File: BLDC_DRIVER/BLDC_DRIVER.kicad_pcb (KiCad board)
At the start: 2 copper layers, 187 parts, among them IC101 DRV8323SRTAR, J1 XT60, J104 691311400103, J2 Conn_01x03_Pin, J3 Conn_01x03_Pin, J4 Conn_01x06_Pin, Q101 BSC146N10LS5ATMA1, Q102 BSC146N10LS5ATMA1, Q103 BSC146N10LS5ATMA1, Q104 BSC146N10LS5ATMA1, Q105 BSC146N10LS5ATMA1, Q106 BSC146N10LS5ATMA1, SW1 SW_Push_Dual_x2, SW2 SW_Push_Dual_x2, SW3 SW_Push_Dual_x2, SW4 SW_Push_Dual_x2, SW5 SW_Push_Dual_x2, U1 LDI1117-3.3H, U2 ESP32-S3-WROOM-1U-N16R2, U3 LMR51610YDBVR, U4 STM32G431RBTx, Y1 24MHz

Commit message: pcb update
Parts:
- moved Q101 119.0 mm to (159.8, 27.8), turned to 180 degrees
- moved Q103 118.2 mm to (173.5, 27.9), turned to 180 degrees
- moved Q105 118.2 mm to (187.9, 27.9), turned to 180 degrees
- moved R121 113.1 mm to (154.1, 36.0), turned to -90 degrees
- moved R122 109.7 mm to (150.1, 36.0), turned to -90 degrees
- moved Q102 105.1 mm to (153.1, 27.2)
- moved Q104 104.8 mm to (167.3, 27.3)
- moved Q106 104.7 mm to (181.7, 27.3)
- moved C105 103.6 mm to (129.9, 76.4), turned to 180 degrees
- moved C103 101.7 mm to (130.1, 31.6), turned to 180 degrees
- moved C106 101.7 mm to (130.0, 61.9), turned to 180 degrees
- moved C104 101.6 mm to (129.9, 47.1), turned to 180 degrees
- moved J104 97.1 mm to (171.2, 17.7)
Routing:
- net (no net): vias 0 -> 4

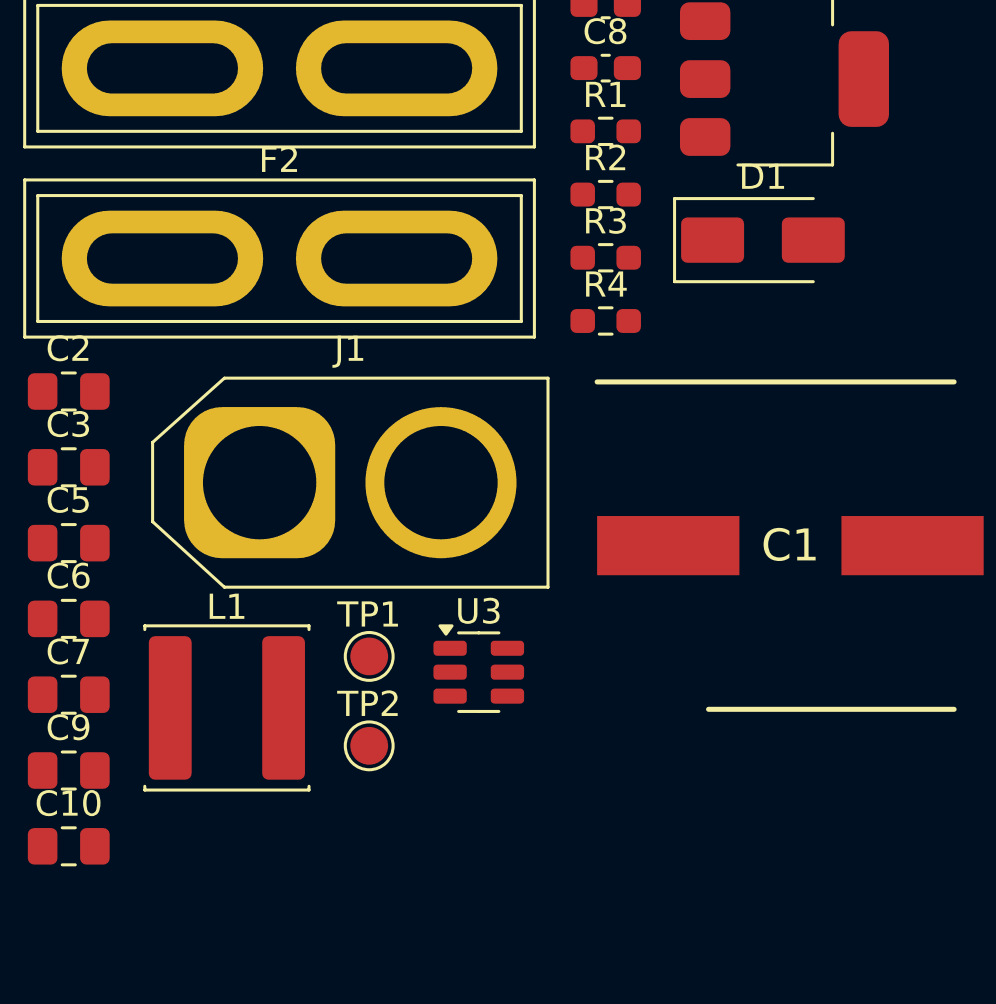
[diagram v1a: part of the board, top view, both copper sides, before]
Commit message: board constraints added
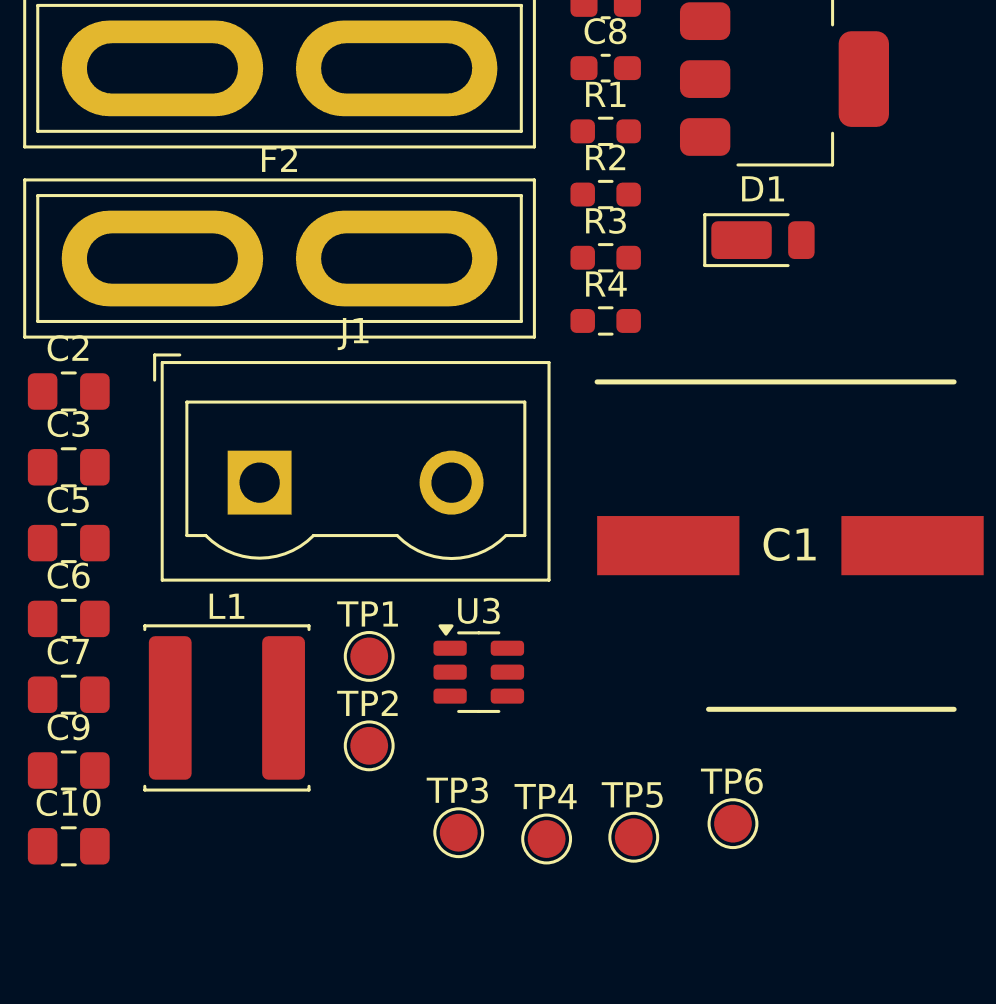
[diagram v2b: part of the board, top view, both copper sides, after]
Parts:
- added TP3: TestPoint, TestPoint:TestPoint_Pad_D1.5mm, F.Cu at (121.5, 164.4)
- added TP4: TestPoint, TestPoint:TestPoint_Pad_D1.5mm, F.Cu at (125.0, 164.7)
- added TP5: TestPoint, TestPoint:TestPoint_Pad_D1.5mm, F.Cu at (128.4, 164.6)
- added TP6: TestPoint, TestPoint:TestPoint_Pad_D1.5mm, F.Cu at (132.4, 164.0)
- D1: value D_Schottky -> SBR3U60P1-7; footprint Diode_SMD:D_SMA -> Diode_SMD:D_PowerDI-123
- J1: value XT60 -> Terminal; footprint Connector_AMASS:AMASS_XT60-M_1x02_P7.20mm_Vertical -> TerminalBlock:TerminalBlock_Wuerth_691311400102_P7.62mm
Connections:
- TP1 pad 1: +5V -> +48V
- TP2 pad 1: +3.3V -> Net-(U3-EN)

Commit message: pre layout
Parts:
- Q101, Q102, Q103, Q104, Q105, Q106: value BSC146N10LS5ATMA1 -> NTMFS4D0N08XT1G; footprint BSC146N10LS5ATMA1:BSC146N10LS5ATMA1 -> NTMFS4D0N08XT1G:NRVTS10100EMFST1G
- R101: value 0R/2W -> 0R/1W; footprint Resistor_SMD:R_2010_5025Metric -> Resistor_SMD:R_0805_2012Metric
- TP106: moved to B.Cu
- moved TP101 207.7 mm to (209.8, 30.2)
- moved TP116 189.2 mm to (199.0, 41.4)
- moved TP120 188.4 mm to (198.2, 68.6)
- moved TP110 187.3 mm to (191.2, 16.8)
- moved TP119 177.8 mm to (186.8, 39.8)
- moved TP106 172.6 mm to (169.0, 14.6)
- moved TP111 169.3 mm to (175.6, 47.4)
- moved TP117 162.9 mm to (172.4, 39.4)
- moved TP114 154.7 mm to (160.0, 43.2)
- moved TP102 150.4 mm to (151.6, 28.4)
- moved R113 148.9 mm to (203.3, 26.1), turned to 90 degrees
- moved TP108 146.8 mm to (141.4, 16.2)
- moved R110 146.6 mm to (195.0, 51.4), turned to 90 degrees
- moved D111 144.4 mm to (192.8, 69.5), turned to -90 degrees
- moved D101 143.7 mm to (197.5, 47.7), turned to 180 degrees
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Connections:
- C119 pad 2: /Motor_driver/SLA -> /Motor_driver/SPA
- C121 pad 2: /Motor_driver/SLB -> /Motor_driver/SPB
- C122 pad 1: /Motor_driver/SLB -> /Motor_driver/SPB
- C123 pad 1: /Motor_driver/SLC -> /Motor_driver/SPC
- C124 pad 1: /Motor_driver/SLA -> /Motor_driver/SPA
- C132 pad 2: /Motor_driver/SLC -> /Motor_driver/SPC
- D107 pad 1: /MCU/SensVB -> /MCU/SensVA
- D107 pad 2: /MCU/SensVA -> /MCU/SensVB
- D109 pad 1: /MCU/PVDDSENSE -> /MCU/SensIC
- D110 pad 1: unconnected-(D110-Pad1) -> /MCU/SensIA
- D110 pad 2: unconnected-(D110-Pad2) -> /MCU/SensIB
- D111 pad 1: unconnected-(D111-Pad1) -> /MCU/PVDDSENSE
- IC101 pad 12: /Motor_driver/SLB -> /Motor_driver/SPB
- IC101 pad 19: /Motor_driver/SLC -> /Motor_driver/SPC
- IC101 pad 9: /Motor_driver/SLA -> /Motor_driver/SPA
- Q102 pad 1: /Motor_driver/SLA -> /Motor_driver/SPA
- Q104 pad 1: /Motor_driver/SLB -> /Motor_driver/SPB
- Q106 pad 1: /Motor_driver/SLC -> /Motor_driver/SPC
- R117 pad 1: /Motor_driver/SLB -> /Motor_driver/SPB
- R118 pad 1: /Motor_driver/SLB -> /Motor_driver/SPB
- R119 pad 1: /Motor_driver/SLC -> /Motor_driver/SPC
- R120 pad 1: /Motor_driver/SLC -> /Motor_driver/SPC
- R121 pad 1: /Motor_driver/SLA -> /Motor_driver/SPA
- R122 pad 1: /Motor_driver/SLA -> /Motor_driver/SPA
- TP114 pad 1: /Motor_driver/SLB -> GND
- TP115 pad 1: /Motor_driver/SLC -> GND
- TP116 pad 1: /Motor_driver/SLA -> GND
- TP117 pad 1: /Motor_driver/SLB -> /Motor_driver/SPB
- TP118 pad 1: /Motor_driver/SLC -> /Motor_driver/SPC
- TP119 pad 1: /Motor_driver/SLA -> /Motor_driver/SPA
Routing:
- net /Motor_driver/SHA: track 0.00 -> 140.3 mm, vias 0 -> 1
- net /Motor_driver/SHC: track 0.00 -> 137.0 mm, vias 0 -> 1
- net /Motor_driver/SHB: track 0.00 -> 116.4 mm, vias 0 -> 1
- net /MCU/TEMP_MOSFET: track 0.00 -> 111.7 mm, vias 0 -> 3
- net GND: track 0.00 -> 102.7 mm, vias 0 -> 16
- net +48V: track 0.00 -> 61.4 mm
- net /Motor_driver/SPC: track 0.00 -> 45.4 mm, vias 0 -> 2
- net Net-(D103-Pad2): track 0.00 -> 38.1 mm
- net /Motor_driver/GLC: track 0.00 -> 37.0 mm
- net /Motor_driver/GHA: track 0.00 -> 34.2 mm
- net /Motor_driver/SPA: track 0.00 -> 33.7 mm, vias 0 -> 2
- net /MCU/SensVA: track 0.00 -> 33.0 mm, vias 0 -> 3
- net /Motor_driver/GHC: track 0.00 -> 31.5 mm
- net /MCU/SensIC: track 0.00 -> 28.8 mm, vias 0 -> 3
- net Net-(D104-Pad2): track 0.00 -> 28.3 mm
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- added copper zone on B.Cu, net +48V
- added copper zone on F.Cu, net +48V
- added copper zone on F.Cu, net /Motor_driver/SHA
- added copper zone on F.Cu, net /Motor_driver/SHB
- added copper zone on F.Cu, net /Motor_driver/SHC
- added copper zone on F.Cu, net /Motor_driver/SPA
- added copper zone on F.Cu, net /Motor_driver/SPB
- added copper zone on F.Cu, net /Motor_driver/SPC
- added copper zone on F.Cu, net GND
- added copper zone on In1.Cu, net GND
- added copper zone on In2.Cu, net GND
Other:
- board outline added: 100 x 100 mm
- copper layers 2 -> 4

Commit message: motor driver layout v1
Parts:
- R105: footprint Resistor_SMD:R_2010_5025Metric -> Resistor_SMD:R_0805_2012Metric
- moved TP104 76.0 mm to (195.0, 48.0)
- moved TP113 72.8 mm to (191.6, 48.0), turned to 90 degrees
- moved F1 61.9 mm to (126.8, 129.2)
- moved F2 59.9 mm to (134.1, 135.8)
- moved TP102 20.2 mm to (157.8, 47.6), turned to 90 degrees
- moved TP103 18.2 mm to (137.4, 47.6)
- moved TP112 15.6 mm to (134.6, 47.6)
- moved D107 8.84 mm to (129.6, 75.9)
- moved D108 7.03 mm to (135.5, 75.9)
- moved D109 5.34 mm to (141.3, 75.9)
- moved C125 5.23 mm to (193.8, 59.8), turned to 90 degrees
- moved R129 4.31 mm to (195.6, 59.8), turned to 90 degrees
- moved D110 4.30 mm to (147.2, 75.9)
- moved TP117 4.02 mm to (172.0, 43.4)
- moved TP119 3.81 mm to (187.0, 43.6)
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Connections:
- D107 pad 1: /MCU/SensVA -> /MCU/SensVB
- D107 pad 2: /MCU/SensVB -> /MCU/SensVA
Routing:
- net +48V: track 61.4 -> 31.5 mm
- net +3.3V: track 0.00 -> 11.8 mm
- net /MCU/CAL: track 0.00 -> 10.6 mm, vias 0 -> 1
- net /MCU/ENABLE: track 0.00 -> 9.79 mm, vias 0 -> 1
- net /MCU/NSCS: track 0.00 -> 9.67 mm, vias 0 -> 1
- net /MCU/SCLK: track 0.00 -> 9.54 mm, vias 0 -> 1
- net /MCU/TEMP_MOSFET: track 111.7 -> 119.1 mm, vias 3 -> 4
- net /MCU/SensVC: track 27.1 -> 21.6 mm
- net /MCU/SensVB: track 27.9 -> 32.8 mm
- net /MCU/NFAULT: track 13.8 -> 9.05 mm, vias 1 -> 0
- net /MCU/SensIC: track 28.8 -> 33.4 mm
- net /Motor_driver/GHC: track 31.5 -> 36.1 mm
- net Net-(D102-Pad2): track 19.9 -> 24.1 mm
- net /MCU/SDI: track 15.6 -> 11.6 mm, vias 1 -> 0
- net /Motor_driver/GHB: track 9.51 -> 13.5 mm
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
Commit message: via update
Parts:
- removed C1: 10uF, EMVY101ARA101MKE0S:CAPAE1300X1400N
- removed C10, C3: 100nF, Capacitor_SMD:C_0805_2012Metric_Pad1.18x1.45mm_HandSolder
- removed C11, C15, C21: 10u, Capacitor_SMD:C_0603_1608Metric_Pad1.08x0.95mm_HandSolder
- removed C12, C13, C14, C18, C19, C20, C22, C23, C8: 100n, Capacitor_SMD:C_0603_1608Metric_Pad1.08x0.95mm_HandSolder
- removed C16, C17: 12p, Capacitor_SMD:C_0603_1608Metric_Pad1.08x0.95mm_HandSolder
- removed C2, C6: 1uF, Capacitor_SMD:C_0805_2012Metric_Pad1.18x1.45mm_HandSolder
- removed C4: 100nF, Capacitor_SMD:C_0603_1608Metric_Pad1.08x0.95mm_HandSolder
- removed C5, C7: 10uF, Capacitor_SMD:C_0805_2012Metric_Pad1.18x1.45mm_HandSolder
- removed C9: 22uF, Capacitor_SMD:C_0805_2012Metric_Pad1.18x1.45mm_HandSolder
- removed D1: SBR3U60P1-7, Diode_SMD:D_PowerDI-123
- removed D2, D3, D4: LED, Diode_SMD:D_0805_2012Metric_Pad1.15x1.40mm_HandSolder
- removed F1, F2: 15A, Fuse:Fuse_Blade_ATO_directSolder
- removed FB1: FerriteBead, Inductor_SMD:L_0805_2012Metric_Pad1.05x1.20mm_HandSolder
- removed J1: Terminal, TerminalBlock:TerminalBlock_Wuerth_691311400102_P7.62mm
- removed J2, J3: Conn_01x03_Pin, Connector_PinHeader_2.54mm:PinHeader_1x03_P2.54mm_Vertical
- removed J4: Conn_01x06_Pin, Connector_PinHeader_2.54mm:PinHeader_1x06_P2.54mm_Vertical
- removed JP1, JP2: Jumper_2_Bridged, Jumper:SolderJumper-2_P1.3mm_Open_TrianglePad1.0x1.5mm
- removed L1: 15uH, Inductor_SMD:L_APV_ANR6045
- removed R1, R2: R, Resistor_SMD:R_0603_1608Metric_Pad0.98x0.95mm_HandSolder
- removed R10, R11, R8, R9: 4.7k, Resistor_SMD:R_0603_1608Metric
- removed R12, R15, R16, R17, R18, R21, R22, R5, R6, R7: 4.7k, Resistor_SMD:R_0603_1608Metric_Pad0.98x0.95mm_HandSolder
- removed R13, R14, R19, R20: 10k, Resistor_SMD:R_0603_1608Metric_Pad0.98x0.95mm_HandSolder
- removed R3: 116k, Resistor_SMD:R_0603_1608Metric_Pad0.98x0.95mm_HandSolder
- removed R4: 22.1k, Resistor_SMD:R_0603_1608Metric_Pad0.98x0.95mm_HandSolder
- removed SW1, SW2, SW3, SW4, SW5: SW_Push_Dual_x2, Button_Switch_SMD:SW_Push_1P1T_NO_CK_KSC7xxJ
- removed TP1, TP2, TP3, TP4, TP5, TP6: TestPoint, TestPoint:TestPoint_Pad_D1.5mm
- removed U1: LDI1117-3.3H, Package_TO_SOT_SMD:SOT-223-3_TabPin2
- removed U3: LMR51610YDBVR, Package_TO_SOT_SMD:SOT-23-6
- removed Y1: 24MHz, Crystal:Crystal_SMD_3225-4Pin_3.2x2.5mm
- moved C120 5.72 mm to (151.0, 27.5)
- moved C131 3.84 mm to (148.4, 27.5)
- moved R136 3.84 mm to (148.0, 22.5)
- moved TP101 3.65 mm to (206.2, 30.8)
- moved R135 2.57 mm to (153.8, 24.4)
- moved TH101 1.44 mm to (164.2, 36.0), turned to 0 degrees
- moved C135 0.43 mm to (184.5, 63.0)
- moved C110 0.36 mm to (178.0, 63.8)
- moved C108 0.32 mm to (178.0, 67.2)
- moved C109 0.15 mm to (181.1, 63.0)
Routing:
- net +48V: track 31.5 -> 67.0 mm, vias 0 -> 55
- net GND: track 99.3 -> 118.5 mm, vias 16 -> 33
- net /MCU/SensVC: track 21.6 -> 34.6 mm
- net /Motor_driver/SPB: track 22.5 -> 30.5 mm
- net /Motor_driver/SPA: track 32.8 -> 39.6 mm
- net /MCU/TEMP_MOSFET: track 119.1 -> 113.5 mm
- net /Motor_driver/SPC: track 43.0 -> 48.3 mm
- net /Motor_driver/SHB: track 116.3 -> 111.2 mm, vias 1 -> 11
- net Net-(D103-Pad2): track 37.6 -> 33.6 mm
- net Net-(C120-Pad2): track 0.00 -> 2.91 mm
- net Net-(C119-Pad1): track 0.00 -> 2.33 mm
- net /MCU/SensIA: track 27.4 -> 26.8 mm
- net /Motor_driver/SHA: track 139.8 -> 139.1 mm, vias 1 -> 10
- net Net-(D105-Pad2): track 29.1 -> 28.6 mm
- net /Motor_driver/SHC: vias 1 -> 12
- added copper zone on B.Cu, net /Motor_driver/SHA
- added copper zone on B.Cu, net /Motor_driver/SHB
- added copper zone on B.Cu, net /Motor_driver/SHC

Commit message: esp/stm/ldo layout
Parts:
- added C1: 10uF, Capacitor_SMD:C_0805_2012Metric_Pad1.18x1.45mm_HandSolder, F.Cu at (234.6, 92.6)
- added C10: 100nF, Capacitor_SMD:C_0805_2012Metric_Pad1.18x1.45mm_HandSolder, F.Cu at (183.6, 104.1)
- added C11: 10u, Capacitor_SMD:C_0603_1608Metric_Pad1.08x0.95mm_HandSolder, F.Cu at (175.2, 89.8)
- added C12: 100n, Capacitor_SMD:C_0603_1608Metric_Pad1.08x0.95mm_HandSolder, F.Cu at (175.2, 91.6)
- added C13: 100n, Capacitor_SMD:C_0603_1608Metric_Pad1.08x0.95mm_HandSolder, F.Cu at (176.4, 97.0)
- added C14: 100n, Capacitor_SMD:C_0603_1608Metric_Pad1.08x0.95mm_HandSolder, F.Cu at (145.8, 108.5)
- added C15: 10u, Capacitor_SMD:C_0603_1608Metric_Pad1.08x0.95mm_HandSolder, F.Cu at (147.6, 108.5)
- added C16: 12p, Capacitor_SMD:C_0603_1608Metric_Pad1.08x0.95mm_HandSolder, F.Cu at (159.4, 77.1)
- added C17: 12p, Capacitor_SMD:C_0603_1608Metric_Pad1.08x0.95mm_HandSolder, F.Cu at (159.4, 83.3)
- added C18: 100n, Capacitor_SMD:C_0603_1608Metric_Pad1.08x0.95mm_HandSolder, F.Cu at (170.2, 97.0)
- added C19: 100n, Capacitor_SMD:C_0603_1608Metric_Pad1.08x0.95mm_HandSolder, F.Cu at (163.9, 97.0)
- added C2: 1uF, Capacitor_SMD:C_0805_2012Metric_Pad1.18x1.45mm_HandSolder, F.Cu at (239.6, 92.5)
- added C20: 100n, Capacitor_SMD:C_0603_1608Metric_Pad1.08x0.95mm_HandSolder, F.Cu at (145.8, 100.5)
- added C21: 10u, Capacitor_SMD:C_0603_1608Metric_Pad1.08x0.95mm_HandSolder, F.Cu at (171.6, 91.6)
- added C22: 100n, Capacitor_SMD:C_0603_1608Metric_Pad1.08x0.95mm_HandSolder, F.Cu at (171.5, 89.9)
- added C23: 100n, Capacitor_SMD:C_0603_1608Metric_Pad1.08x0.95mm_HandSolder, F.Cu at (145.8, 104.2)
- added C3: 100nF, Capacitor_SMD:C_0805_2012Metric_Pad1.18x1.45mm_HandSolder, F.Cu at (239.6, 95.5)
- added C4: 100nF, Capacitor_SMD:C_0603_1608Metric_Pad1.08x0.95mm_HandSolder, F.Cu at (244.2, 92.2)
- added C5: 10uF, Capacitor_SMD:C_0805_2012Metric_Pad1.18x1.45mm_HandSolder, F.Cu at (239.6, 98.5)
- added C6: 1uF, Capacitor_SMD:C_0805_2012Metric_Pad1.18x1.45mm_HandSolder, F.Cu at (239.6, 101.5)
- added C7: 10uF, Capacitor_SMD:C_0805_2012Metric_Pad1.18x1.45mm_HandSolder, F.Cu at (189.2, 98.2)
- added C8: 100n, Capacitor_SMD:C_0603_1608Metric_Pad1.08x0.95mm_HandSolder, F.Cu at (186.8, 98.4)
- added C9: 22uF, Capacitor_SMD:C_0805_2012Metric_Pad1.18x1.45mm_HandSolder, F.Cu at (180.8, 104.1)
- added D1: SBR3U60P1-7, Diode_SMD:D_PowerDI-123, F.Cu at (250.0, 98.2)
- added D2: LED, Diode_SMD:D_0805_2012Metric_Pad1.15x1.40mm_HandSolder, F.Cu at (153.8, 86.8)
- added D3: LED, Diode_SMD:D_0805_2012Metric_Pad1.15x1.40mm_HandSolder, F.Cu at (153.7, 90.4)
- added D4: LED, Diode_SMD:D_0805_2012Metric_Pad1.15x1.40mm_HandSolder, F.Cu at (153.7, 94.0)
- added F1: 15A, Fuse:Fuse_Blade_ATO_directSolder, F.Cu at (276.1, 137.2)
- added F2: 15A, Fuse:Fuse_Blade_ATO_directSolder, F.Cu at (276.0, 127.5)
- added FB1: FerriteBead, Inductor_SMD:L_0805_2012Metric_Pad1.05x1.20mm_HandSolder, F.Cu at (173.4, 93.6)
- added J1: Terminal, TerminalBlock:TerminalBlock_Wuerth_691311400102_P7.62mm, F.Cu at (209.3, 106.5)
- added J2: Conn_01x03_Pin, Connector_PinHeader_2.54mm:PinHeader_1x03_P2.54mm_Vertical, F.Cu at (130.0, 85.6)
- added J3: Conn_01x03_Pin, Connector_PinHeader_2.54mm:PinHeader_1x03_P2.54mm_Vertical, F.Cu at (140.4, 85.5)
- added J4: Conn_01x06_Pin, Connector_PinHeader_2.54mm:PinHeader_1x06_P2.54mm_Vertical, F.Cu at (147.4, 94.5)
- added JP1: Jumper_2_Bridged, Jumper:SolderJumper-2_P1.3mm_Open_TrianglePad1.0x1.5mm, F.Cu at (135.3, 81.9)
- added JP2: Jumper_2_Bridged, Jumper:SolderJumper-2_P1.3mm_Open_TrianglePad1.0x1.5mm, F.Cu at (135.3, 89.8)
- added L1: 15uH, Inductor_SMD:L_APV_ANR6045, F.Cu at (236.2, 86.0)
- added R1: R, Resistor_SMD:R_0603_1608Metric_Pad0.98x0.95mm_HandSolder, F.Cu at (256.4, 95.3)
- added R10: 4.7k, Resistor_SMD:R_0603_1608Metric_Pad0.98x0.95mm_HandSolder, F.Cu at (158.0, 86.8)
- added R11: 10k, Resistor_SMD:R_0603_1608Metric_Pad0.98x0.95mm_HandSolder, F.Cu at (170.2, 98.8)
- added R12: 10k, Resistor_SMD:R_0603_1608Metric_Pad0.98x0.95mm_HandSolder, F.Cu at (163.9, 98.8)
- added R13: 4.7k, Resistor_SMD:R_0603_1608Metric_Pad0.98x0.95mm_HandSolder, F.Cu at (171.4, 110.9)
- added R14: 4.7k, Resistor_SMD:R_0603_1608Metric_Pad0.98x0.95mm_HandSolder, F.Cu at (165.0, 111.0)
- added R15: 4.7k, Resistor_SMD:R_0603_1608Metric_Pad0.98x0.95mm_HandSolder, F.Cu at (157.9, 90.3)
- added R16: 4.7k, Resistor_SMD:R_0603_1608Metric_Pad0.98x0.95mm_HandSolder, F.Cu at (158.1, 93.9)
- added R17: 10k, Resistor_SMD:R_0603_1608Metric_Pad0.98x0.95mm_HandSolder, F.Cu at (147.7, 100.5)
- added R18: 10k, Resistor_SMD:R_0603_1608Metric_Pad0.98x0.95mm_HandSolder, F.Cu at (147.6, 104.2)
- added R19: 4.7k, Resistor_SMD:R_0603_1608Metric_Pad0.98x0.95mm_HandSolder, F.Cu at (158.6, 110.8)
- added R2: R, Resistor_SMD:R_0603_1608Metric_Pad0.98x0.95mm_HandSolder, F.Cu at (256.4, 97.8)
- added R20: 4.7k, Resistor_SMD:R_0603_1608Metric_Pad0.98x0.95mm_HandSolder, F.Cu at (152.2, 110.9)
- added R3: 116k, Resistor_SMD:R_0603_1608Metric_Pad0.98x0.95mm_HandSolder, F.Cu at (256.4, 100.3)
- added R4: 22.1k, Resistor_SMD:R_0603_1608Metric_Pad0.98x0.95mm_HandSolder, F.Cu at (256.4, 102.8)
- added R5: 4.7k, Resistor_SMD:R_0603_1608Metric_Pad0.98x0.95mm_HandSolder, F.Cu at (176.4, 98.8)
- added R6: 4.7k, Resistor_SMD:R_0603_1608Metric_Pad0.98x0.95mm_HandSolder, F.Cu at (163.9, 74.6)
- added R7: 4.7k, Resistor_SMD:R_0603_1608Metric_Pad0.98x0.95mm_HandSolder, F.Cu at (177.7, 110.8)
- added R8: 4.7k, Resistor_SMD:R_0603_1608Metric, F.Cu at (126.2, 90.7)
- added R9: 4.7k, Resistor_SMD:R_0603_1608Metric, F.Cu at (140.6, 90.6)
- added SW1: SW_Push, Button_Switch_SMD:SW_Tactile_SPST_NO_Straight_CK_PTS636Sx25SMTRLFS, F.Cu at (176.2, 104.8)
- added SW2: SW_Push, Button_Switch_SMD:SW_Tactile_SPST_NO_Straight_CK_PTS636Sx25SMTRLFS, F.Cu at (170.7, 104.8)
- added SW3: SW_Push, Button_Switch_SMD:SW_Tactile_SPST_NO_Straight_CK_PTS636Sx25SMTRLFS, F.Cu at (165.1, 104.8)
- added SW4: SW_Push, Button_Switch_SMD:SW_Tactile_SPST_NO_Straight_CK_PTS636Sx25SMTRLFS, F.Cu at (159.2, 104.7)
- added SW5: SW_Push, Button_Switch_SMD:SW_Tactile_SPST_NO_Straight_CK_PTS636Sx25SMTRLFS, F.Cu at (153.7, 104.8)
- added TP1: TestPoint, TestPoint:TestPoint_Pad_D1.5mm, F.Cu at (243.4, 83.9)
- added TP2: TestPoint, TestPoint:TestPoint_Pad_D1.5mm, F.Cu at (243.4, 87.5)
- added TP3: TestPoint, TestPoint:TestPoint_Pad_D1.5mm, F.Cu at (246.9, 83.9)
- added TP4: TestPoint, TestPoint:TestPoint_Pad_D1.5mm, F.Cu at (246.9, 87.5)
- added TP5: TestPoint, TestPoint:TestPoint_Pad_D1.5mm, F.Cu at (183.8, 100.2)
- added TP6: TestPoint, TestPoint:TestPoint_Pad_D1.5mm, F.Cu at (183.6, 110.4)
- added U1: LDI1117-3.3H, Package_TO_SOT_SMD:SOT-223-3_TabPin2, F.Cu at (189.1, 105.2)
- added U3: LMR51610YDBVR, Package_TO_SOT_SMD:SOT-23-6, F.Cu at (255.6, 85.0)
- added Y1: 24MHz, Crystal:Crystal_SMD_3225-4Pin_3.2x2.5mm, F.Cu at (159.3, 79.9)
- moved U4 14.5 mm to (170.4, 81.2)
- moved U2 2.60 mm to (134.0, 102.2), turned to 180 degrees
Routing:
- net +3.3V: track 11.8 -> 202.9 mm, vias 0 -> 4
- net /MCU/BOOT: track 0.00 -> 37.0 mm, vias 0 -> 2
- net /MCU/PVDDSENSE: track 16.9 -> 52.6 mm, vias 2 -> 4
- net /MCU/RX_ESP32: track 0.00 -> 32.4 mm, vias 0 -> 1
- net /MCU/TX_ESP32: track 0.00 -> 31.7 mm, vias 0 -> 1
- net /MCU/NRST: track 0.00 -> 31.4 mm, vias 0 -> 2
- net /MCU/FUNC_BTN1: track 0.00 -> 26.9 mm, vias 0 -> 2
- net /MCU/FUNC_BTN2: track 0.00 -> 25.8 mm, vias 0 -> 2
- net /MCU/ESP_EN: track 0.00 -> 17.0 mm
- net /MCU/SensIC: track 33.2 -> 48.7 mm, vias 3 -> 5
- net /MCU/SensIB: track 29.5 -> 41.8 mm, vias 3 -> 5
- net /MCU/SensIA: track 26.8 -> 37.6 mm, vias 3 -> 5
- net /MCU/RCC_OSC_OUT: track 0.00 -> 9.78 mm
- net +5V: track 0.00 -> 8.60 mm
- net /MCU/GH3: track 0.00 -> 7.85 mm, vias 0 -> 2
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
